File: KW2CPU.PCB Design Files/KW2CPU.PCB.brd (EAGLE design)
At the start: 50 x 30 mm, 67 parts, among them IC1 25AA080SN, J1 DF12_M, J2 MOLEX55560-0207, J3 MMCX_VERT, U1 MKW21D, U3 RF6555, U5 F-ANTENNA, X1 32KHZ, X2 32MHZ

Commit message: KW2CPU.PCB.v1.1 Release
Fixed Gerbers (omitted layer), fixed BOM suffixes (see ECO), tented vias
and antenna holes in Eagle (and Gerbers), added Stackup -> Layer in Fab
notes.
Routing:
- added copper zone on layer 15, net +3V3
- removed copper zone on layer 3, net +3V3
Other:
- board text added: "KW2CPU.PCB.v1.1"
- board text added: "R.S 12/19/14"
- board text removed: "KW2CPU.PCB.v1.0"
- board text removed: "R.S 11/22/14"

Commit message: Fixed PTC5 net name
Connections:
- net PTC5/LLWU_P8/SPI0_PCS0/UART1_TX/FTM0_CH3/CMP1_OUT renamed PTC5/LLWU_P9/SPI0_SCK/LPTMR0_ALT2/I2S0_RXDO/CMP0_OUT
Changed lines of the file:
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@@
 <wire x1="6.35" y1="11.049" x2="6.477" y2="10.922" width="0.1778" layer="15"/>
 </signal>
-<signal name="PTC5/LLWU_P8/SPI0_PCS0/UART1_TX/FTM0_CH3/CMP1_OUT">
+<signal name="PTC5/LLWU_P9/SPI0_SCK/LPTMR0_ALT2/I2S0_RXDO/CMP0_OUT">
 <contactref element="U1" pad="P$5"/>
 <contactref element="J1" pad="P$24"/>

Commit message: KW2CPU.PCB.v1.2 Release
DNP Voltage regulator (BOM change + schematic attribute, ECO),
incremented silkscreen to v1.2, fixed name on BOM filr (added .BOM)
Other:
- board text added: "KW2CPU.PCB.v1.2"
- board text added: "R.S 2/6/15"
- board text removed: "KW2CPU.PCB.v1.1"
- board text removed: "R.S 12/19/14"
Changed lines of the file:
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@@
 <layer number="251" name="SMDround" color="12" fill="11" visible="no" active="no"/>
 <layer number="254" name="cooling" color="7" fill="1" visible="yes" active="yes"/>
-<layer number="255" name="255" color="7" fill="1" visible="no" active="yes"/>
+<layer number="255" name="255" color="7" fill="1" visible="yes" active="yes"/>
 </layers>
 <board>
@@
 <wire x1="41.512" y1="-15.238" x2="-8.488" y2="-15.238" width="0.4064" layer="20"/>
 <wire x1="-8.488" y1="-15.238" x2="-8.488" y2="14.762" width="0.4064" layer="20"/>
-<text x="21.467" y="11.287" size="1.778" layer="22" font="vector" ratio="15" rot="SMR0">KW2CPU.PCB.v1.1</text>
+<text x="21.467" y="11.287" size="1.778" layer="22" font="vector" ratio="15" rot="SMR0">KW2CPU.PCB.v1.2</text>
 <text x="2.036003125" y="4.75665625" size="1.016" layer="22" font="vector" ratio="15" rot="SMR0">JTAG</text>
-<text x="21.3273" y="9.19911875" size="1.016" layer="22" font="vector" ratio="15" rot="SMR0">R.S 12/19/14</text>
+<text x="21.3273" y="9.19911875" size="1.016" layer="22" font="vector" ratio="15" rot="SMR0">R.S 2/6/15</text>
 <rectangle x1="1.64465" y1="-12.970503125" x2="1.98246875" y2="-12.952728125" layer="22"/>
 <rectangle x1="17.895571875" y1="-12.970503125" x2="18.233390625" y2="-12.952728125" layer="22"/>
@@
 <attribute name="MFGN" value="Microchip" x="4.949" y="-9.89" size="1.778" layer="27" rot="R90" display="off"/>
 <attribute name="MFGP" value="MCP1804T-3302I/DB" x="4.949" y="-9.89" size="1.778" layer="27" rot="R90" display="off"/>
+<attribute name="NOTES" value="DNP" x="4.949" y="-9.89" size="1.778" layer="27" rot="R90" display="off"/>
 </element>
 <element name="R7" library="GW-devices" package="RFMD0402" value="0" x="26.54810625" y="6.61238125" smashed="yes" rot="R90">

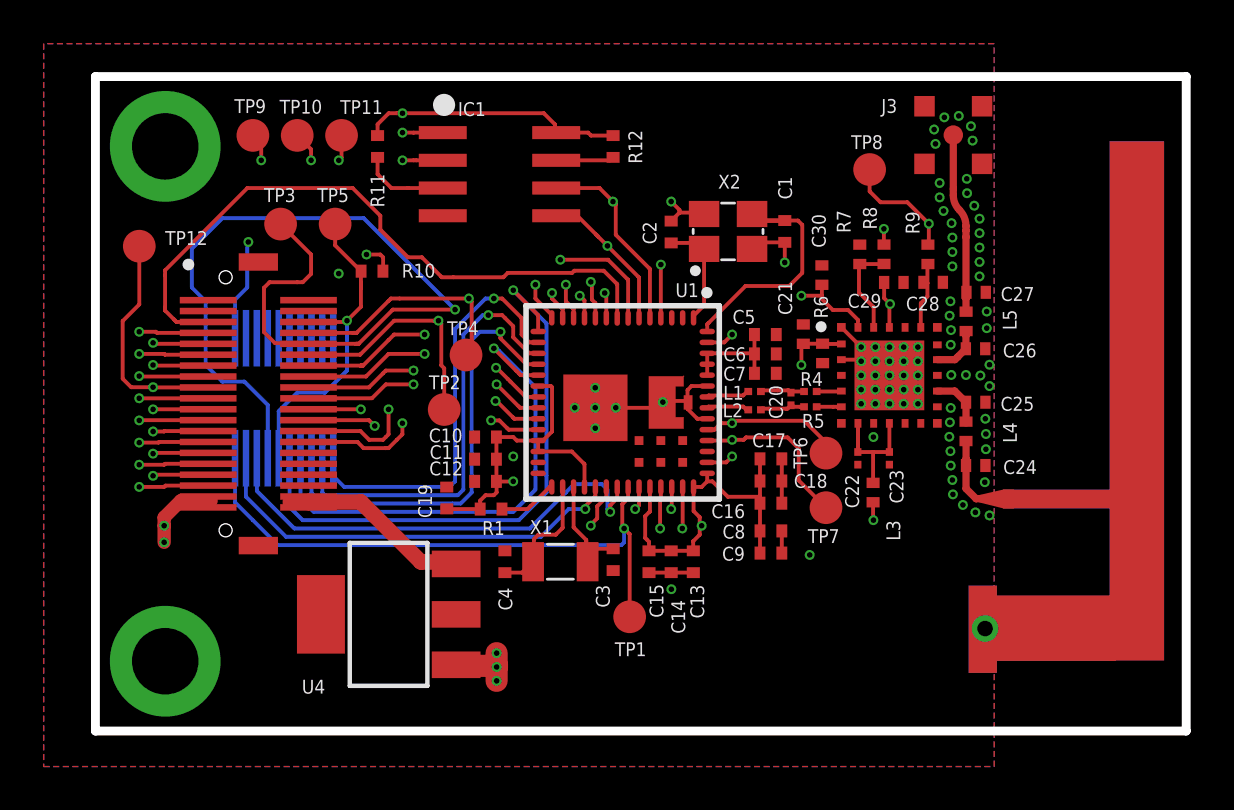
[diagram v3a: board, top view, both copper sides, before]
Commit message: First cut at v1.3 (antenna diversity)
* Antenna diversity
* ISO layouts
* More TPs
* Axial anchors
* Remvoe top JTAG connector
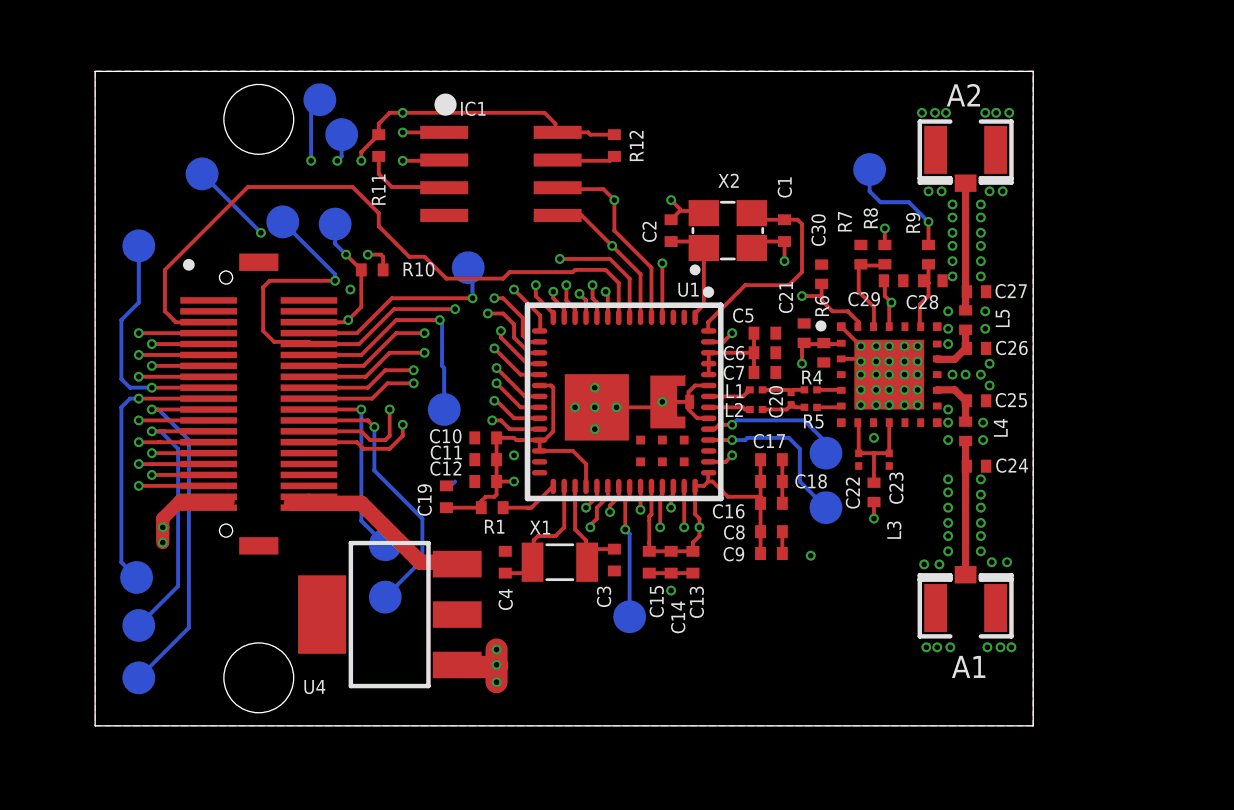
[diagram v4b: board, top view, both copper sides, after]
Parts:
- removed J2: MOLEX55560-0207, KW2:MOLEX55560-0207
- removed J3: MMCX_VERT, KW2:MMCX_VERT
- removed U5: F-ANTENNA, KW2:F_ANT_RFMD
- added A1, A2: (no value), adafruit:U.FL
- added TP13, TP14, TP15, TP16, TP17: PTR1TP15R, testpad:TP15R
- added U$1: CODESHELF-LOGOSMALL, GW-devices:CODESHELF-LOGO-SMALL
- C24, C26, C27: value (none) -> 0pF
- L5: value 0 -> 0nH
- moved TP4 4.00 mm to (8.60, 6.00), flipped to the bottom
- moved TP9 2.92 mm to (-3.60, 10.3), flipped to the bottom
- moved TP10 1.94 mm to (1.80, 13.7), flipped to the bottom
- moved TP3 0.14 mm to (0.10, 8.10), flipped to the bottom
- moved L1 0.10 mm to (21.8, 0.40)
- moved R1 0.08 mm to (9.70, -5.00)
- moved C25 0.08 mm to (31.9, -0.10)
- moved R4 0.08 mm to (24.3, 0.40)
- moved C29 0.08 mm to (28.1, 5.40)
- moved U1 0.07 mm to (11.8, 3.85)
- moved R12 0.07 mm to (15.3, 11.6)
- moved C22 0.07 mm to (26.5, -2.80)
- moved L2 0.07 mm to (21.8, -0.50)
- moved C28 0.07 mm to (29.9, 5.40)
- moved R11 0.07 mm to (4.50, 11.6)
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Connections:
- removed net F_ANT: C24.P$1, L4.P$2, U5.P$1
- removed net MMCX_ANT: C27.P$1, J3.P$1, L5.P$1
- new net U.FL.ANT1: A1.3, C24.P$1, L4.P$2
- new net U.FL.ANT2: A2.3, C27.P$1, L5.P$1
- net !RESET: no longer J2.P$10
- net +3V3: no longer J2.P$1
- net GND: now also A1.1, A1.2, A2.1, A2.2; no longer J2.P$15, J2.P$17, J2.P$19, J2.P$3, J2.P$5, J2.P$9, J3.P$2, J3.P$3, J3.P$4, J3.P$5, U5.P$2, U5.P$3, U5.P$4
- net PTA0/JTAG_TCLK/SWD_CLK/EZP_CLK/!UART0_CTS/!UART0_COL/FTM0_CH5: no longer J2.P$4
- net PTA1/JTAG_TDI/EZP_DI/UART0/RX/FTM0_CH6: no longer J2.P$8
- net PTA2/JTAG_TDO/TRACE?SWO/EZP_DO/UART0_TX/FTM0_CH7: no longer J2.P$6
- net PTA3/JTAG_TMS/SWD_DIO/UART0_RTS/FTM0_CH0: no longer J2.P$2
- net PTC4/LLWU_P8/SPI0_PCS0/UART1_TX/FTM0_CH3/CMP1_OUT: now also TP13.TP
- net PTC5/LLWU_P9/SPI0_SCK/LPTMR0_ALT2/I2S0_RXDO/CMP0_OUT: now also TP14.TP
- net PTE0/MADC0_SE10/SPI1_PCS1/UART1_TX/MTRACE_CLKOUT/I2C1_SDA/RTC_CLKOUT: now also TP15.TP; no longer J2.P$12
- net PTE1/LLWU_P0/MADC0_SE11/SPI1_SOUT/UART1_RX/MTRACE_D3/I2C1_SCL/SPI1_SIN: now also TP16.TP; no longer J2.P$20
- net PTE2/LLWU_P1/MADC0_DP1/SPI1_SCK/!UART1_CTS!/MTRACE_D2: no longer J2.P$18
- net PTE3/MADC0_DM1/SPI1_SIN/!UART1_RTS!/MTRACE_D1/SPI1_SOUT: now also TP17.TP; no longer J2.P$16
- net PTE4/LLWU_P2/SPI1_PCS0/MTRACE_D0: no longer J2.P$14
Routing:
- net PTA1/JTAG_TDI/EZP_DI/UART0/RX/FTM0_CH6: track 59.7 -> 35.7 mm, vias 2 -> 3
- net PTA3/JTAG_TMS/SWD_DIO/UART0_RTS/FTM0_CH0: track 50.7 -> 29.3 mm
- net PTA0/JTAG_TCLK/SWD_CLK/EZP_CLK/!UART0_CTS/!UART0_COL/FTM0_CH5: track 45.3 -> 24.4 mm
- net PTE4/LLWU_P2/SPI1_PCS0/MTRACE_D0: track 44.8 -> 24.3 mm
- net PTA2/JTAG_TDO/TRACE?SWO/EZP_DO/UART0_TX/FTM0_CH7: track 49.2 -> 28.8 mm
- net PTE2/LLWU_P1/MADC0_DP1/SPI1_SCK/!UART1_CTS!/MTRACE_D2: track 46.7 -> 30.0 mm
- net PTE0/MADC0_SE10/SPI1_PCS1/UART1_TX/MTRACE_CLKOUT/I2C1_SDA/RTC_CLKOUT: track 54.4 -> 38.9 mm
- net PTC5/LLWU_P9/SPI0_SCK/LPTMR0_ALT2/I2S0_RXDO/CMP0_OUT: track 30.9 -> 40.3 mm
- net !RESET: track 42.6 -> 34.2 mm, vias 2 -> 3
- net MMCX_ANT: track 8.23 -> 0.00 mm
- net PTE3/MADC0_DM1/SPI1_SIN/!UART1_RTS!/MTRACE_D1/SPI1_SOUT: track 40.9 -> 33.6 mm
- net PTC4/LLWU_P8/SPI0_PCS0/UART1_TX/FTM0_CH3/CMP1_OUT: track 36.5 -> 42.9 mm
- net U.FL.ANT1: track 0.00 -> 6.21 mm
- net U.FL.ANT2: track 0.00 -> 5.89 mm
- net F_ANT: track 2.84 -> 0.00 mm
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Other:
- board size 50 x 30 mm -> 43 x 30 mm
- board text added: "KW2CPU.v1.3"
- board text removed: "KW2CPU.PCB.v1.2"
- board text removed: "R.S 2/6/15"

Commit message: Layout changes
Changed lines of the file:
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@@
 <wire x1="11.875" y1="-2.4" x2="11.875" y2="-1.9" width="0.1778" layer="1"/>
 <wire x1="22" y1="-2.8" x2="22" y2="-3.8" width="0.1778" layer="1"/>
-<wire x1="27.7" y1="5.3" x2="27.6555" y2="5.4" width="0" layer="19" extent="1-16"/>
 <wire x1="22" y1="-6.1" x2="22" y2="-7.1" width="0.1778" layer="1"/>
 <polygon width="0.254" layer="15" thermals="no">
@@
 <wire x1="13.4" y1="-2.4" x2="14" y2="-3" width="0.1778" layer="1"/>
 <wire x1="9.9" y1="-12.3" x2="8.1" y2="-12.3" width="1.016" layer="1"/>
-<wire x1="8.1" y1="-12.3" x2="8.0988" y2="-12.2114" width="0" layer="19" extent="1-16"/>
 <wire x1="9.2" y1="-5" x2="9.2" y2="-4.7" width="0.1778" layer="1"/>
 <wire x1="9.2" y1="-4.7" x2="9.4" y2="-4.5" width="0.1778" layer="1"/>
@@
 <wire x1="3.7" y1="11.3" x2="4.5" y2="12.1" width="0.1778" layer="1"/>
 <wire x1="12.1" y1="-1.9" x2="11.875" y2="-1.9" width="0" layer="19" extent="1-1"/>
+<wire x1="8.0988" y1="-12.2114" x2="8.1" y2="-12.3" width="0" layer="19" extent="1-1"/>
 </signal>
 <signal name="EXTAL_32M">
@@
 <contactref element="L3" pad="P$1"/>
 <wire x1="27.9" y1="-1.1" x2="27.9" y2="-2.5" width="0.1778" layer="1"/>
-<wire x1="26.46" y1="-1.1" x2="26.5" y2="-2.5" width="0" layer="19" extent="1-16"/>
 <wire x1="26.5" y1="-2.5" x2="26.5" y2="-2.51045" width="0.1778" layer="1"/>
 <wire x1="26.46" y1="-1.1" x2="26.5" y2="-1.1" width="0.1778" layer="1"/>
@@
 <wire x1="31.4" y1="4.0445" x2="31.4" y2="4.8" width="0.332740625" layer="1"/>
 <wire x1="31.4" y1="4.8" x2="31.5" y2="4.8" width="0.332740625" layer="1"/>
-<wire x1="31.5" y1="4.8" x2="31.4555" y2="4.9" width="0" layer="19" extent="1-16"/>
 <wire x1="31.4555" y1="4.9" x2="31.4" y2="4.9" width="0.332740625" layer="1"/>
 <wire x1="31.4" y1="4.9" x2="31.4" y2="8.7" width="0.332740625" layer="1"/>
 <contactref element="A2" pad="3"/>
 <wire x1="31.4" y1="9.875" x2="31.4" y2="8.7" width="0.3327" layer="1"/>
+<wire x1="31.4" y1="4.8" x2="31.4555" y2="4.8" width="0.4064" layer="1"/>
+<wire x1="31.4555" y1="4.8" x2="31.4555" y2="4.9" width="0.4064" layer="1"/>
 </signal>
 <signal name="ANT_A">
@@
 <wire x1="11.875" y1="2.6" x2="11.4" y2="2.6" width="0.1778" layer="1"/>
 <wire x1="11.4" y1="2.6" x2="11.1" y2="2.9" width="0.1778" layer="1"/>
-<wire x1="7.8" y1="-4" x2="8" y2="-3.8" width="0.1778" layer="16"/>
 <contactref element="TP16" pad="TP"/>
 <wire x1="-5.9" y1="-0.5" x2="-5.6" y2="-0.5" width="0.1778" layer="16"/>
@@
 <wire x1="-4.2" y1="-1.9" x2="-4.2" y2="-10.5" width="0.1778" layer="16"/>
 <wire x1="-4.2" y1="-10.5" x2="-6.5" y2="-12.8" width="0.1778" layer="16"/>
-<wire x1="11.4" y1="2.6" x2="8" y2="-3.8" width="0" layer="19" extent="1-16"/>
 </signal>
 <signal name="PTE2/LLWU_P1/MADC0_DP1/SPI1_SCK/!UART1_CTS!/MTRACE_D2">
@@
 <wire x1="14.5" y1="-4.5" x2="14" y2="-5" width="0.1778" layer="1"/>
 <contactref element="TP4" pad="TP"/>
-<wire x1="8.6" y1="6" x2="8.3" y2="5.9" width="0" layer="19" extent="1-16"/>
-<wire x1="8.6" y1="6" x2="8.8" y2="5.9" width="0" layer="19" extent="1-16"/>
 <wire x1="8.8" y1="5.9" x2="8.8" y2="4.6" width="0.1778" layer="16"/>
+<wire x1="8.8" y1="5.9" x2="8.6" y2="6" width="0" layer="19" extent="16-16"/>
 </signal>
 <signal name="PTA1/JTAG_TDI/EZP_DI/UART0/RX/FTM0_CH6">
@@
 <wire x1="1.3" y1="-4.8" x2="0.6" y2="-4.8" width="0.1778" layer="1"/>
 <wire x1="6.4" y1="-7.5" x2="8.1" y2="-7.5" width="0.7112" layer="1"/>
-<wire x1="8.0988" y1="-7.5886" x2="8.1" y2="-7.6" width="0" layer="19" extent="1-16"/>
+<wire x1="8.1" y1="-7.6" x2="8.0988" y2="-7.5886" width="0" layer="19" extent="1-1"/>
 </signal>
 <signal name="C_LNA">
@@
 <wire x1="27.2" y1="4.2" x2="27.2" y2="3.3" width="0.1778" layer="1"/>
 <wire x1="27.2" y1="3.3" x2="27.18" y2="3.3" width="0.1778" layer="1"/>
-<wire x1="26.5" y1="6.2" x2="26.6" y2="6.1555" width="0" layer="19" extent="1-1"/>
+<wire x1="26.5" y1="6.2" x2="26.6" y2="6.2" width="0.4064" layer="1"/>
+<wire x1="26.6" y1="6.2" x2="26.6" y2="6.1555" width="0.4064" layer="1"/>
 </signal>
 <signal name="GND">
@@
 <wire x1="18.7" y1="0.3" x2="18.7" y2="-0.15" width="0.1778" layer="1"/>
 <wire x1="18.7" y1="-0.15" x2="18.75" y2="-0.15" width="0.1778" layer="1"/>
-<wire x1="17.4" y1="0.2" x2="17.5" y2="-0.15" width="0" layer="19" extent="1-16"/>
 <wire x1="17.5" y1="-0.15" x2="18.75" y2="-0.15" width="0.1778" layer="1"/>
-<wire x1="17.4" y1="-0.4" x2="17.5" y2="-0.15" width="0" layer="19" extent="1-16"/>
 <wire x1="23.1" y1="7.2" x2="21.9" y2="7.2" width="0.1778" layer="1"/>
 <wire x1="21.9" y1="7.2" x2="21.6" y2="6.9" width="0.254" layer="1"/>
@@
 <wire x1="19.1" y1="-0.9" x2="18.7" y2="-0.5" width="0.1778" layer="1"/>
 <wire x1="14.5" y1="-0.4" x2="17.4" y2="-0.4" width="0.1778" layer="1"/>
-<wire x1="17.4" y1="0.2" x2="17.4" y2="0.3" width="0" layer="19" extent="1-16"/>
-<wire x1="17.4" y1="0.3" x2="17.5625" y2="0.35" width="0" layer="19" extent="1-16"/>
 <wire x1="18.75" y1="-0.15" x2="18.7" y2="-0.2" width="0.1778" layer="1"/>
 <wire x1="18.3" y1="8.6" x2="19.4" y2="8.6" width="0.1778" layer="1"/>

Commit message: KW2 v1.3 revisions
The first big slug of KW2 revisions.
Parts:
- added R2: 0, GW-devices:RFMD0402
- added RFI1, RFI2, RFI3, RFI4, RFI5, RFI6, TP18: PTR1TP15R, testpad:TP15R
- C1, C2: value 12pF -> 9pF
- C24: value 0pF -> 0.5pF
- C25: value 0.2pF -> 0.0pF
- C26: value 0pF -> 1.0pF
- L4: value 2.2nH -> 1.2nH
- L5: value 0nH -> 1.5nH
- moved TP13 9.83 mm to (-2.30, 0.10)
- moved TP14 9.24 mm to (-0.60, -1.60)
- moved TP6 6.11 mm to (24.7, -8.60)
- moved TP7 4.38 mm to (22.5, -8.60)
- moved TP17 2.90 mm to (-6.50, -7.50)
- moved TP15 1.30 mm to (-6.50, -9.50)
- moved A1 1.02 mm to (32.4, -9.80)
- moved A2 1.02 mm to (32.4, 11.2)
- moved C25 1.02 mm to (32.9, -0.30)
- moved C27 1.02 mm to (32.9, 4.70)
- moved L4 1.02 mm to (32.4, -1.70)
- moved L5 1.02 mm to (32.4, 3.40)
- moved C24 1.02 mm to (32.9, -3.30)
- moved C26 1.02 mm to (32.9, 2.10)
- moved U$1 0.76 mm to (33.8, -14.6)
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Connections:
- removed net C_LNA: R7.P$1, R8.P$2, U3.P$23
- new net GPIO1: J1.P$30, U1.P$2
- new net GPIO2: J1.P$32, R7.P$1, R8.P$2, U1.P$3, U3.P$23
- net ANTSEL: now also R2.P$1
- net GND: now also RFI1.TP, RFI2.TP, RFI3.TP, RFI4.TP, RFI5.TP, RFI6.TP
- net PTE2/LLWU_P1/MADC0_DP1/SPI1_SCK/!UART1_CTS!/MTRACE_D2: now also TP17.TP
- net PTE3/MADC0_DM1/SPI1_SIN/!UART1_RTS!/MTRACE_D1/SPI1_SOUT: now also TP18.TP; no longer TP17.TP
- net TX_SWITCH: now also R2.P$2
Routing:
- net GPIO2: track 0.00 -> 39.3 mm, vias 0 -> 3
- net GPIO1: track 0.00 -> 24.7 mm, vias 0 -> 2
- net ANTSEL: track 3.39 -> 10.8 mm
- net PTE2/LLWU_P1/MADC0_DP1/SPI1_SCK/!UART1_CTS!/MTRACE_D2: track 30.0 -> 37.1 mm
- net TX_SWITCH: track 22.1 -> 28.4 mm
- net PTC5/LLWU_P9/SPI0_SCK/LPTMR0_ALT2/I2S0_RXDO/CMP0_OUT: track 40.3 -> 35.7 mm
- net C_LNA: track 4.57 -> 0.00 mm
- net PTE0/MADC0_SE10/SPI1_PCS1/UART1_TX/MTRACE_CLKOUT/I2C1_SDA/RTC_CLKOUT: track 38.9 -> 40.6 mm
- net RX_SWITCH: track 28.8 -> 30.1 mm
- net +3V3: track 65.2 -> 66.4 mm
- net PTE3/MADC0_DM1/SPI1_SIN/!UART1_RTS!/MTRACE_D1/SPI1_SOUT: track 33.6 -> 34.7 mm
- net ANT1: track 2.58 -> 3.58 mm
- net ANT2: track 2.44 -> 3.43 mm
- net PTE1/LLWU_P0/MADC0_SE11/SPI1_SOUT/UART1_RX/MTRACE_D3/I2C1_SCL/SPI1_SIN: track 42.7 -> 43.4 mm
- net GND: track 19.4 -> 19.3 mm, vias 97 -> 104
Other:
- board size 43 x 30 mm -> 44 x 30 mm
